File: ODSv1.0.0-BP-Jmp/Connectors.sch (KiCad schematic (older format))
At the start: 2 parts, among them J2 Conn_02x60_Odd_Even, J3 Conn_02x60_Odd_Even

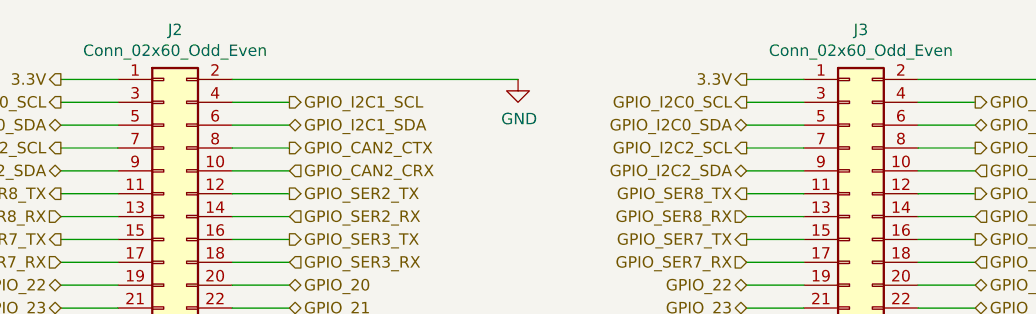
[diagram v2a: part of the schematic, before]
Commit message: Add 2k pullups within DCS selectors (#17), bump BP-Jmp to 0.2.0
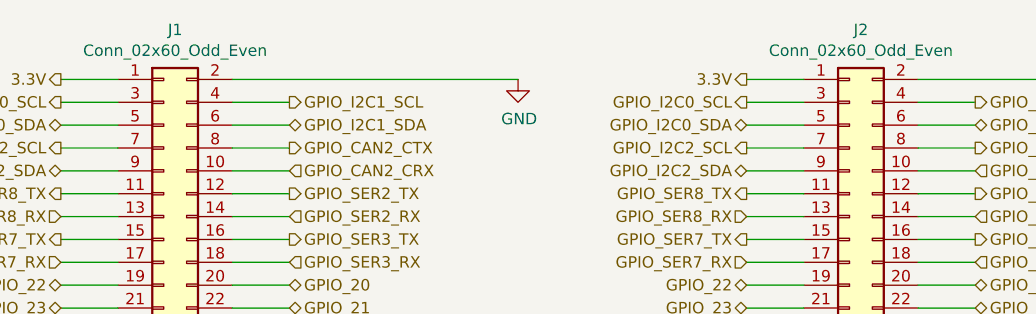
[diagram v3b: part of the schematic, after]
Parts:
- renumbered J2 to J1, J3 to J2
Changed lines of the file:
@@
 $Descr USLetter 11000 8500
 encoding utf-8
-Sheet 4 9
+Sheet 3 9
 Title "Breakout Plane for Jumper Wires"
-Date "2021-03-10"
-Rev "v0.1.1"
+Date "2021-03-11"
+Rev "v0.2.0"
 Comp "Prakash Lab/Octopi Team"
 Comment1 "Designer: Ethan Li"
@@
 AR Path="/60EAE366" Ref="J?"  Part="1"
 AR Path="/60C51399/60EAE366" Ref="J?"  Part="1"
-AR Path="/60C51399/60E9531F/60EAE366" Ref="J2"  Part="1"
-F 0 "J2" H 2500 7067 50  0000 C CNN
+AR Path="/60C51399/60E9531F/60EAE366" Ref="J1"  Part="1"
+F 0 "J1" H 2500 7067 50  0000 C CNN
 F 1 "Conn_02x60_Odd_Even" H 2500 6976 50  0000 C CNN
 F 2 "Backbone_Connector_Hirose:Hirose_FX20_FX20-120P-0.5SV_2x60_P0.50mm_Vertical" H 2450 3950 50  0001 C CNN
@@
 AR Path="/61296724" Ref="J?"  Part="1"
 AR Path="/60C51399/61296724" Ref="J?"  Part="1"
-AR Path="/60C51399/60E9531F/61296724" Ref="J3"  Part="1"
-F 0 "J3" H 5500 7067 50  0000 C CNN
+AR Path="/60C51399/60E9531F/61296724" Ref="J2"  Part="1"
+F 0 "J2" H 5500 7067 50  0000 C CNN
 F 1 "Conn_02x60_Odd_Even" H 5500 6976 50  0000 C CNN
 F 2 "Backbone_Connector_Hirose:Hirose_FX20_FX20-120S-0.5SV_2x60_P0.50mm_Vertical" H 5450 3950 50  0001 C CNN
